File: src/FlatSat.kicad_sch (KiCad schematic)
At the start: 32 parts, among them J1 LiPo, J2 Conn_01x04_MountingPin, J3 Conn_01x04_MountingPin, J4 Conn_02x03_Odd_Even, J5 Conn_01x12_Pin, J6 Conn_01x04_MountingPin, J7 Micro_SD_Card_Det2, U1 Xiao, U2 MPU-6050 / 6500, U3 BME280 /BMP280, U4 MiniMeter

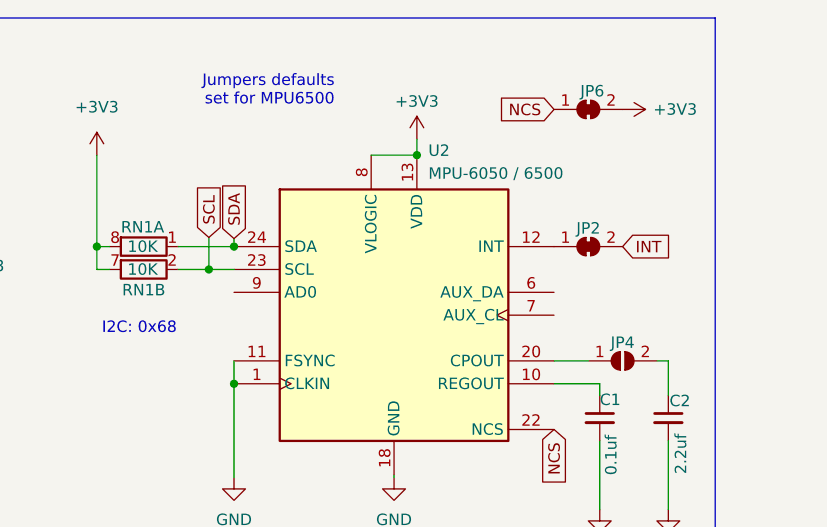
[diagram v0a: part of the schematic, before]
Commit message: update routing for MPU6050 + fix traces + jumpers
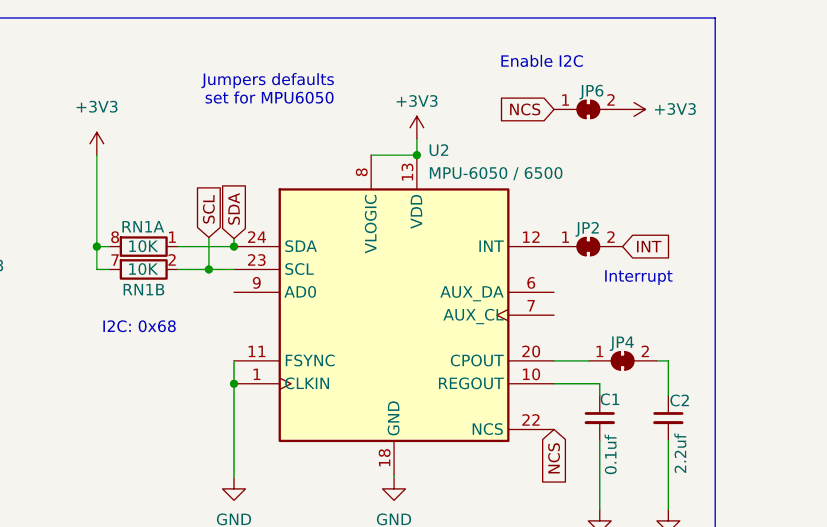
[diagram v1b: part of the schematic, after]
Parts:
- removed JP4: SolderJumper_2_Open, Jumper:SolderJumper-2_P1.3mm_Open_RoundedPad1.0x1.5mm, symbol Jumper:SolderJumper_2_Open
- added JP4: SolderJumper_2_Bridged, Jumper:SolderJumper-2_P1.3mm_Bridged_RoundedPad1.0x1.5mm, symbol Jumper:SolderJumper_2_Bridged
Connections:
- net at U2.20 (CPOUT): now also JP4.1 (A)
- net at C2.1: now also JP4.2 (B)
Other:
- note added: "Enable I2C"
- note added: "Interrupt"
- note added: "Jumpers defaults set for MPU6050"
- note removed: "Jumpers defaults set for MPU6500"
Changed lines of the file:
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@@
 		)
 	)
-	(text "Jumpers defaults\nset for MPU6500"
+	(text "Jumpers defaults\nset for MPU6050"
 		(exclude_from_sim no)
 		(at 239.776 23.368 0)
@@
 		)
 	)
+	(text "Interrupt"
+		(exclude_from_sim no)
+		(at 277.368 44.196 0)
+		(effects
+			(font
+				(size 1.27 1.27)
+			)
+			(justify right)
+		)
+	)
 	(text "Battery + Power"
 		(exclude_from_sim no)
@@
 		)
 	)
+	(text "Enable I2C"
+		(exclude_from_sim no)
+		(at 267.462 20.32 0)
+		(effects
+			(font
+				(size 1.27 1.27)
+			)
+			(justify right)
+		)
+	)
 	(text "Qwiic Connector"
 		(exclude_from_sim no)
@@
 	)
 	(symbol
-		(lib_id "Jumper:SolderJumper_2_Open")
+		(lib_id "Jumper:SolderJumper_2_Bridged")
 		(at 271.78 53.34 0)
 		(unit 1)
@@
 			)
 		)
-		(property "Value" "SolderJumper_2_Open"
+		(property "Value" "SolderJumper_2_Bridged"
 			(at 271.78 49.53 0)
 			(effects
@@
 			)
 		)
-		(property "Footprint" "Jumper:SolderJumper-2_P1.3mm_Open_RoundedPad1.0x1.5mm"
+		(property "Footprint" "Jumper:SolderJumper-2_P1.3mm_Bridged_RoundedPad1.0x1.5mm"
 			(at 271.78 53.34 0)
 			(effects
@@
 			)
 		)
-		(property "Description" "Solder Jumper, 2-pole, open"
+		(property "Description" ""
 			(at 271.78 53.34 0)
 			(effects
@@
 					(size 1.27 1.27)
 				)
-				(hide yes)
 			)
 		)
-		(pin "2"
-		)
 		(pin "1"
 		)
+		(pin "2"
+		)
 		(instances
-			(project ""
+			(project "FlatSat"
 				(path "/af1e39d1-0976-42d3-af26-3ed9fdefdeb1"
 					(reference "JP4")
